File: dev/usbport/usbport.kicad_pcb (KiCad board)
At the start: 2 copper layers, 12 x 33.5 mm, 9 parts, among them J1 USB_C_Receptacle_USB2.0_16P, J2 Conn_01x04_MountingPin, U1 TPD4E05U06DQAR

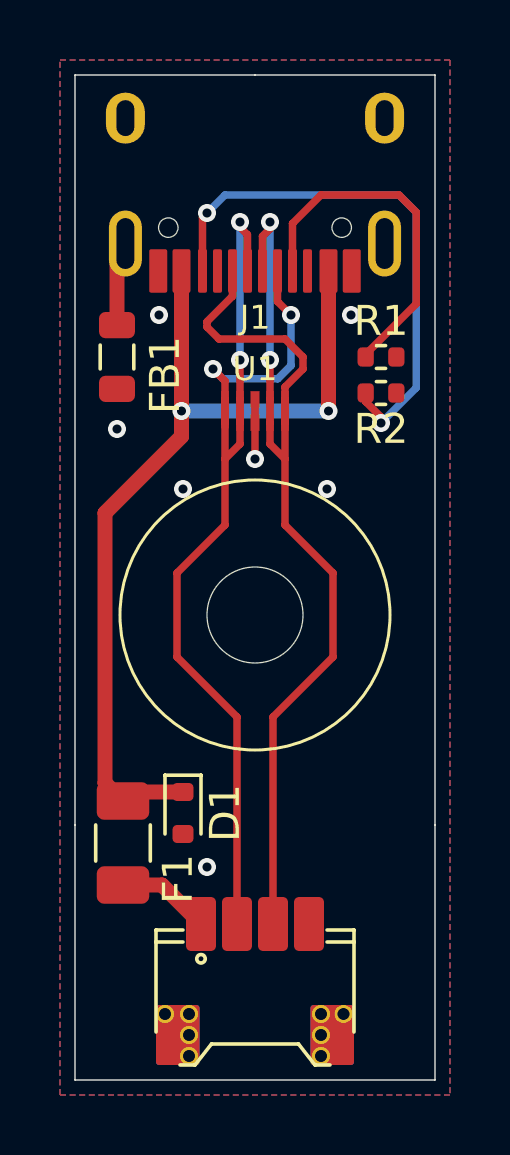
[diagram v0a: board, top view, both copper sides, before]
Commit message: Add initial usbport rev 0 - from the unified daughterboard project
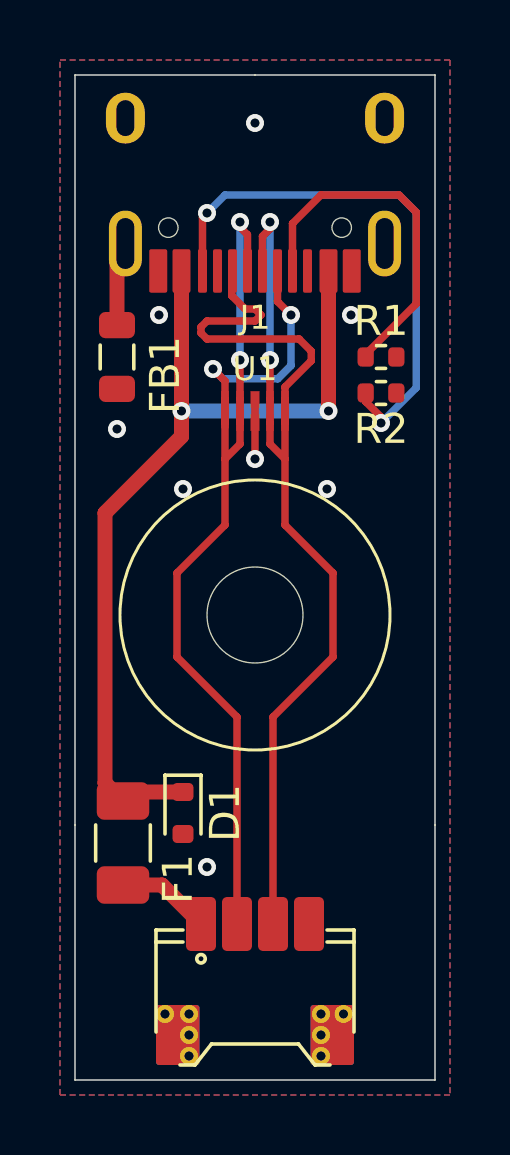
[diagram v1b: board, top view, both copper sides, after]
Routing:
- net D+: track 37.1 -> 39.9 mm
- net GND: vias 7 -> 8
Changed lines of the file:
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@@
 			(plot_on_all_layers_selection 0x00000000_00000000_00000000_00000000)
 			(disableapertmacros no)
-			(usegerberextensions no)
-			(usegerberattributes yes)
-			(usegerberadvancedattributes yes)
-			(creategerberjobfile yes)
+			(usegerberextensions yes)
+			(usegerberattributes no)
+			(usegerberadvancedattributes no)
+			(creategerberjobfile no)
 			(dashed_line_dash_ratio 12.000000)
 			(dashed_line_gap_ratio 3.000000)
@@
 			(outputformat 1)
 			(mirror no)
-			(drillshape 1)
+			(drillshape 0)
 			(scaleselection 1)
-			(outputdirectory "")
+			(outputdirectory "/home/matthew/repos/nesceptor/dev/usbport/gbr/")
 		)
 	)
@@
 			(at -3 0.8)
 			(size 0.6 0.6)
-			(drill 0.4)
+			(drill 0.3)
 			(layers "*.Cu")
 			(remove_unused_layers no)
@@
 			(at -2.2 0.8)
 			(size 0.6 0.6)
-			(drill 0.4)
+			(drill 0.3)
 			(layers "*.Cu")
 			(remove_unused_layers no)
@@
 			(at -2.2 1.5)
 			(size 0.6 0.6)
-			(drill 0.4)
+			(drill 0.3)
 			(layers "*.Cu")
 			(remove_unused_layers no)
@@
 			(at -2.2 2.2)
 			(size 0.6 0.6)
-			(drill 0.4)
+			(drill 0.3)
 			(layers "*.Cu")
 			(remove_unused_layers no)
@@
 			(at 2.2 0.8)
 			(size 0.6 0.6)
-			(drill 0.4)
+			(drill 0.3)
 			(layers "*.Cu")
 			(remove_unused_layers no)
@@
 			(at 2.2 1.5)
 			(size 0.6 0.6)
-			(drill 0.4)
+			(drill 0.3)
 			(layers "*.Cu")
 			(remove_unused_layers no)
@@
 			(at 2.2 2.2)
 			(size 0.6 0.6)
-			(drill 0.4)
+			(drill 0.3)
 			(layers "*.Cu")
 			(remove_unused_layers no)
@@
 			(at 2.95 0.8)
 			(size 0.6 0.6)
-			(drill 0.4)
+			(drill 0.3)
 			(layers "*.Cu")
 			(remove_unused_layers no)
@@
 		)
 		(fp_line
+			(start 3.75 -7.5)
+			(end 4.5 -7.5)
+			(stroke
+				(width 0.15)
+				(type solid)
+			)
+			(layer "F.CrtYd")
+		)
+		(fp_line
 			(start 3.75 -8.5)
 			(end 3.75 -7.5)
@@
 		(fp_line
 			(start -4.5 -7.5)
-			(end 4.5 -7.5)
+			(end -3.75 -7.5)
 			(stroke
 				(width 0.15)
@@
 			(pinfunction "GND")
 			(pintype "passive")
+			(clearance 0.1)
 		)
 		(pad "A4" smd roundrect
@@
 			(pinfunction "VBUS")
 			(pintype "passive")
+			(clearance 0.1)
 		)
 		(pad "A5" smd roundrect
@@
 			(pinfunction "GND")
 			(pintype "passive")
+			(clearance 0.1)
 		)
 		(pad "B4" smd roundrect
@@
 			(pinfunction "VBUS")
 			(pintype "passive")
+			(clearance 0.1)
 		)
 		(pad "B5" smd roundrect
@@
 	)
 	(via
+		(at 92 74.6)
+		(size 0.6)
+		(drill 0.3)
+		(layers "F.Cu" "B.Cu")
+		(free yes)
+		(net 4)
+	)
+	(via
 		(at 92 85.8)
 		(size 0.6)
@@
 	)
 	(segment
+		(start 93.874 82.203168)
+		(end 93.470832 81.8)
+		(width 0.25)
+		(layer "F.Cu")
+		(net 6)
+	)
+	(segment
 		(start 92.5 83.815)
 		(end 92.5 84.585)
@@
 	)
 	(segment
-		(start 90.8 81.8)
-		(end 90.4 81.4)
-		(width 0.25)
-		(layer "F.Cu")
-		(net 6)
-	)
-	(segment
-		(start 90.4 81.4)
-		(end 90.4 81.225)
-		(width 0.25)
-		(layer "F.Cu")
-		(net 6)
-	)
-	(segment
-		(start 91.25 80.375)
-		(end 91.25 79.5325)
-		(width 0.25)
-		(layer "F.Cu")
-		(net 6)
-	)
-	(segment
 		(start 93 85.8)
 		(end 93 88)
@@
 	)
 	(segment
+		(start 90.2 81.4)
+		(end 90.4 81.2)
+		(width 0.25)
+		(layer "F.Cu")
+		(net 6)
+	)
+	(segment
+		(start 92 80.8)
+		(end 91.666952 80.8)
+		(width 0.25)
+		(layer "F.Cu")
+		(net 6)
+	)
+	(segment
 		(start 92.5 77.9)
 		(end 92.5 78.125003)
@@
 	)
 	(segment
-		(start 93.6 82.8)
-		(end 93.6 82.4)
+		(start 93.874 82.526)
+		(end 93.874 82.203168)
 		(width 0.25)
 		(layer "F.Cu")
@@
 	)
 	(segment
-		(start 90.4 81.225)
-		(end 91.25 80.375)
+		(start 90.4 81.2)
+		(end 92 81.2)
 		(width 0.25)
 		(layer "F.Cu")
@@
 	)
 	(segment
-		(start 93 83.4)
-		(end 93.6 82.8)
+		(start 92.2 81)
+		(end 92 80.8)
 		(width 0.25)
 		(layer "F.Cu")
@@
 	)
 	(segment
-		(start 93 81.8)
-		(end 90.8 81.8)
+		(start 93.470832 81.8)
+		(end 90.4 81.8)
+		(width 0.25)
+		(layer "F.Cu")
+		(net 6)
+	)
+	(segment
+		(start 90.4 81.8)
+		(end 90.2 81.6)
 		(width 0.25)
 		(layer "F.Cu")
@@
 	(segment
 		(start 93 83.815)
-		(end 93 83.4)
-		(width 0.25)
-		(layer "F.Cu")
-		(net 6)
-	)
-	(segment
-		(start 93 83.815)
 		(end 93 84.585)
 		(width 0.25)
@@
 	)
 	(segment
-		(start 93.6 82.4)
-		(end 93 81.8)
+		(start 92 81.2)
+		(end 92.2 81)
+		(width 0.25)
+		(layer "F.Cu")
+		(net 6)
+	)
+	(segment
+		(start 90.2 81.6)
+		(end 90.2 81.4)
+		(width 0.25)
+		(layer "F.Cu")
+		(net 6)
+	)
+	(segment
+		(start 91.25 80.15)
+		(end 91.25 79.5325)
 		(width 0.25)
 		(layer "F.Cu")
@@
 	)
 	(segment
+		(start 91.666952 80.8)
+		(end 91.226 80.359048)
+		(width 0.25)
+		(layer "F.Cu")
+		(net 6)
+	)
+	(segment
+		(start 93 83.4)
+		(end 93.874 82.526)
+		(width 0.25)
+		(layer "F.Cu")
+		(net 6)
+	)
+	(segment
+		(start 91.226 80.359048)
+		(end 91.226 80.174)
+		(width 0.25)
+		(layer "F.Cu")
+		(net 6)
+	)
+	(segment
+		(start 91.226 80.174)
+		(end 91.25 80.15)
+		(width 0.25)
+		(layer "F.Cu")
+		(net 6)
+	)
+	(segment
 		(start 92.5 85.3)
 		(end 92.5 84.585)
 		(width 0.25)
 		(layer "F.Cu")
+		(net 6)
+	)
+	(segment
+		(start 93 83.815)
+		(end 93 83.4)
+		(width 0.25)
+		(layer "F.Cu")
